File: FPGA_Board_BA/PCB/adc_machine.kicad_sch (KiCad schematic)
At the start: 15 parts, among them U11 LTC2320-16_CMOS

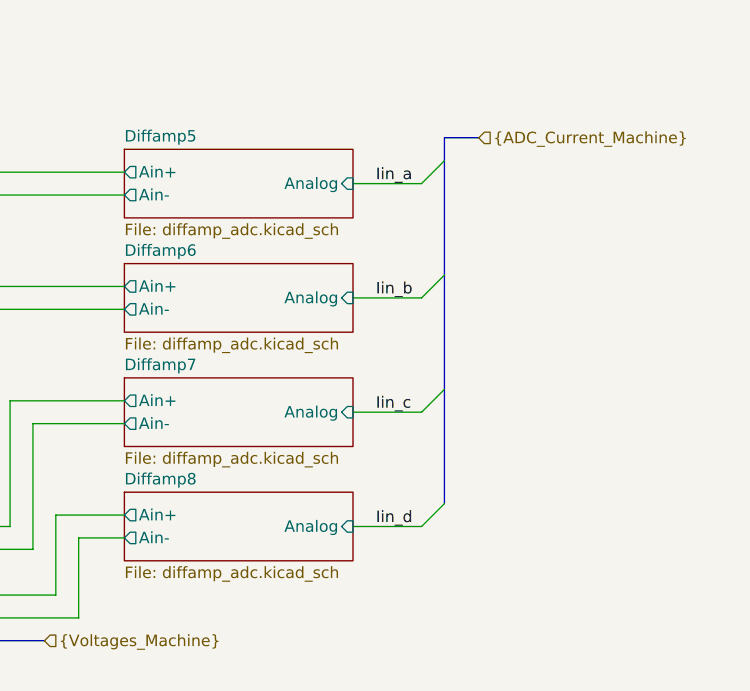
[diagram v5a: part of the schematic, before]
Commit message: final layout almost ready (onlypower is left)
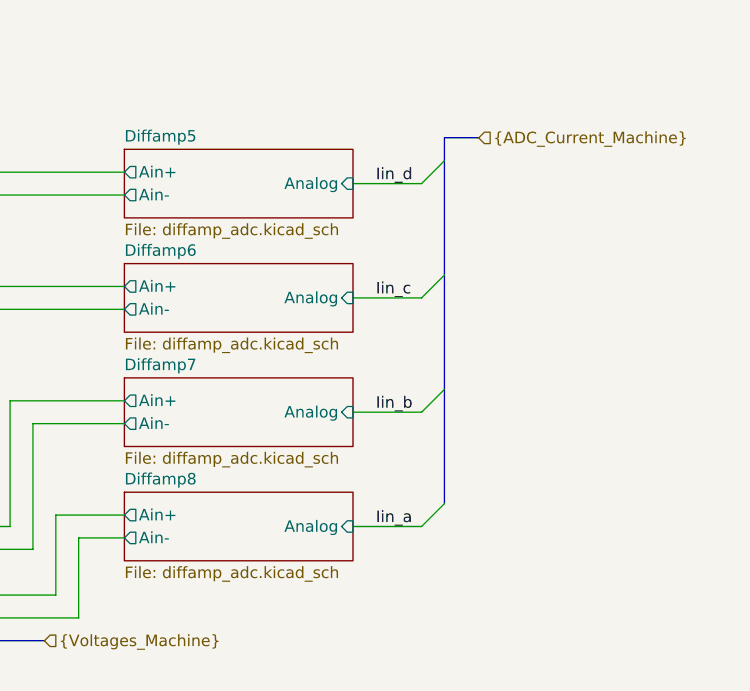
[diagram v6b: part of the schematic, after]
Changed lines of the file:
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@@
 	)
 	(label "Iin_d"
-		(at 247.65 101.6 0)
+		(at 247.65 63.5 0)
 		(effects
 			(font
@@
 	)
 	(label "Iin_a"
-		(at 247.65 63.5 0)
+		(at 247.65 101.6 0)
 		(effects
 			(font
@@
 	)
 	(label "Iin_b"
-		(at 247.65 76.2 0)
+		(at 247.65 88.9 0)
 		(effects
 			(font
@@
 	)
 	(label "Iin_c"
-		(at 247.65 88.9 0)
+		(at 247.65 76.2 0)
 		(effects
 			(font
